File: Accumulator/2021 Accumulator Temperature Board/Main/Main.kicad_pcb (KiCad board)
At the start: 2 copper layers, 63.4 x 45.4 mm, 51 parts, among them J1 Conn_02x06_Odd_Even, J1001 Conn_01x06, J1002 M3, J1003 Conn_01x04, J1004 Conn_01x04, J1005 M3, J1006 M3, J2 Conn_02x06_Odd_Even, J3 M3, U20002 ISO1050, U20003 RFM-0505S, U2001 STM32F072R8Tx, U3001 LP2985-3.3

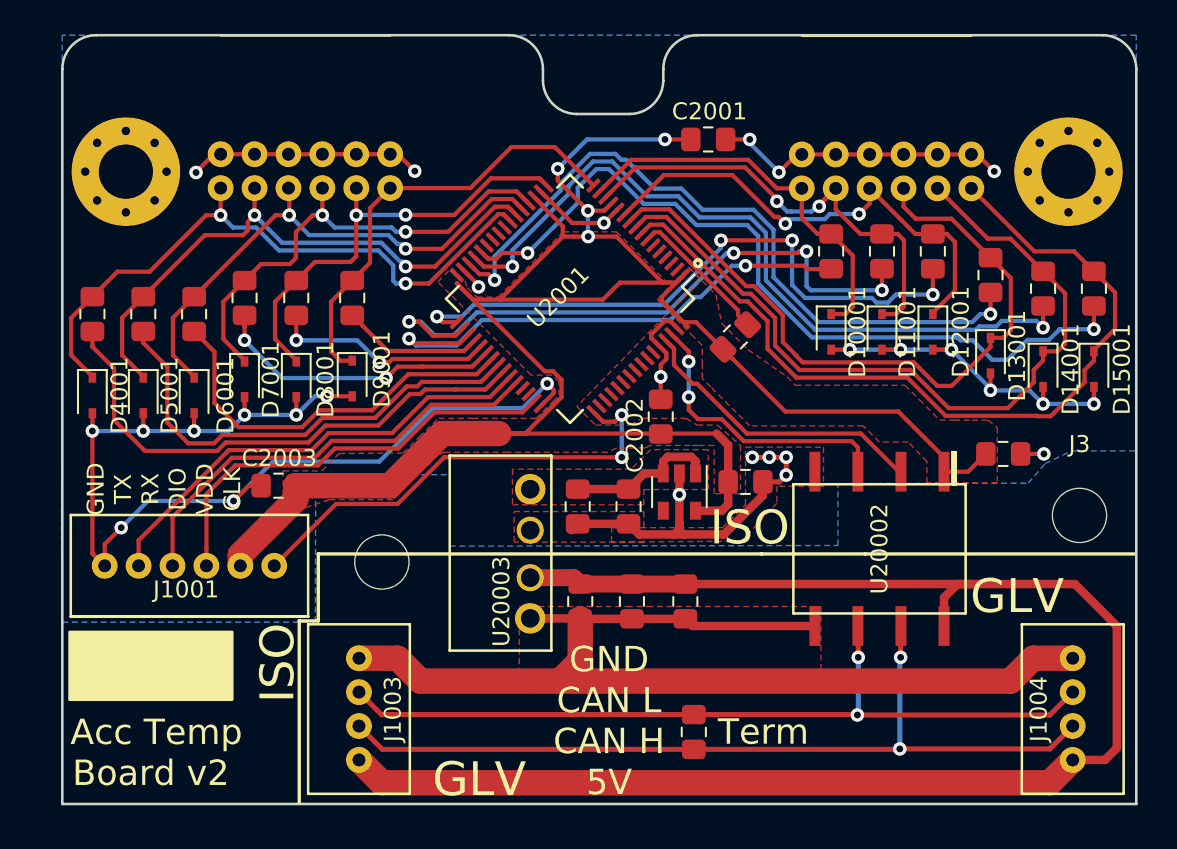
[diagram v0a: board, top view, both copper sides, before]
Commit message: Changes to Thermoboard
Disconnected mounting holes from GND, changed Zener package to hand-soldering.
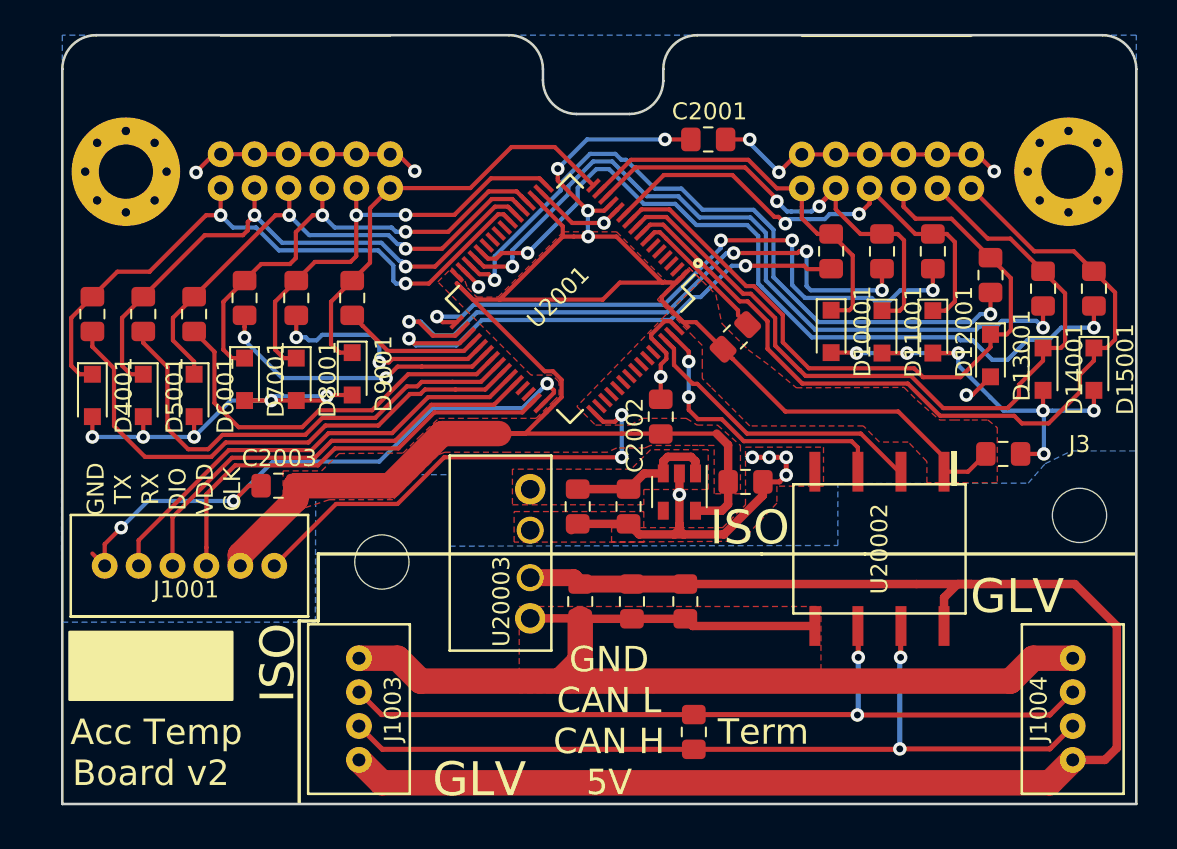
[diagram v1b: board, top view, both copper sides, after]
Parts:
- removed G***: LOGO, KiCAD Graphics:KiCAD_Duck_Graphic_v3
- removed G***: LOGO, KiCAD Graphics:UOWM_LOGO_v1
- D10001, D11001, D12001, D13001, D14001, D15001, D4001, D5001, D6001, D7001, D8001, D9001: footprint Diode_SMD:D_SOD-323 -> Diode_SMD:D_SOD-323_HandSoldering
- moved D9001 0.27 mm to (12.8, -38.1)
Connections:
- J1002 pad 1: GND -> Net-(J1002-Pad1)
- J1006 pad 1: GND -> Net-(J1006-Pad1)
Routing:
- net GND: track 155.7 -> 157.0 mm, vias 29 -> 28
- net /MUX Interface/ADC_11: track 49.9 -> 50.9 mm
- net /MUX Interface/PU_3: track 18.0 -> 17.1 mm
- net /MUX Interface/PU_4: track 13.3 -> 14.1 mm
- net /MUX Interface/ADC_5: track 27.1 -> 26.5 mm

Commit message: Changes to Thermoboard Mounting
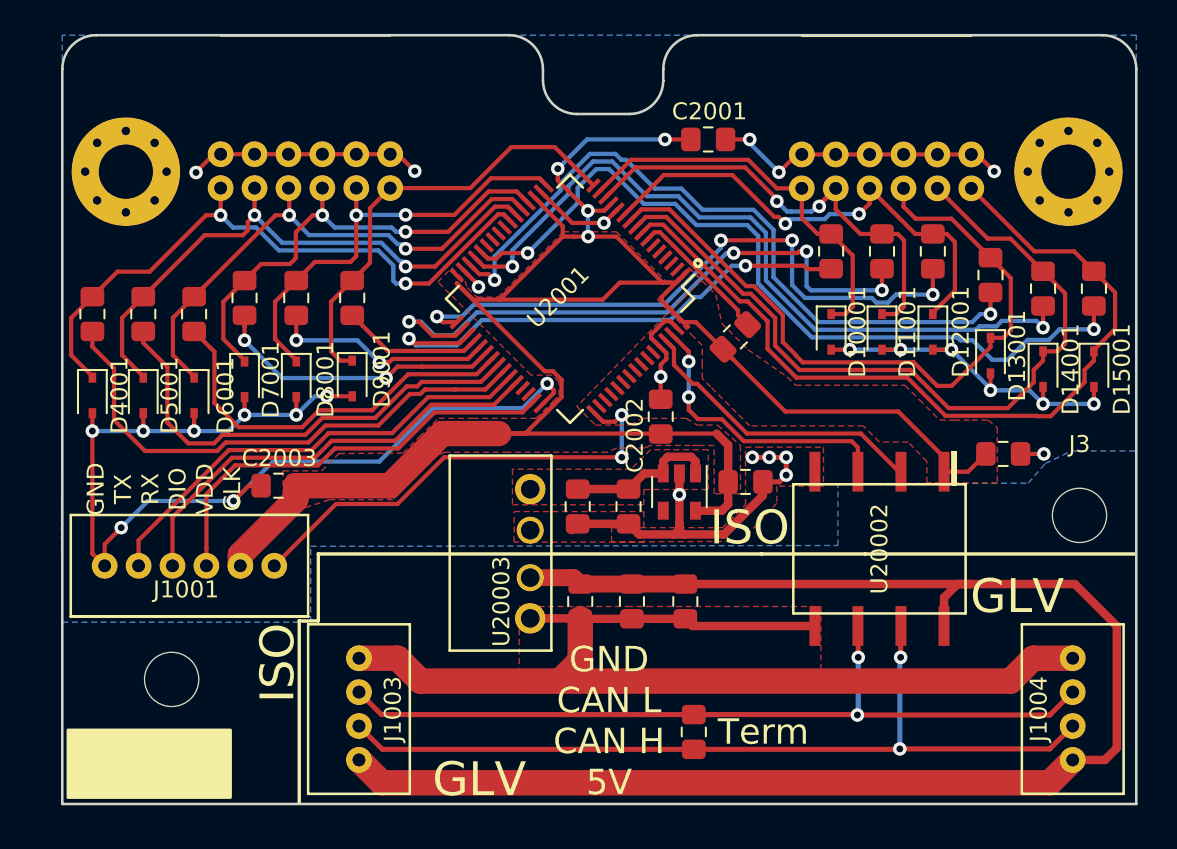
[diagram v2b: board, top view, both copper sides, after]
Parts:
- added G***: LOGO, KiCAD Graphics:UOWM_LOGO_v1, B.Cu at (38.9, -25.3)
- added G***: LOGO, KiCAD Graphics:KiCAD_Duck_Graphic_v3, B.Cu at (-1.98, -14.8)
- D10001, D11001, D12001, D13001, D14001, D15001, D4001, D5001, D6001, D7001, D8001, D9001: footprint Diode_SMD:D_SOD-323_HandSoldering -> Diode_SMD:D_SOD-323
- moved J1005 14.2 mm to (2.10, -20.1)
- moved D9001 0.27 mm to (12.8, -37.9)
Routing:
- net GND: track 157.0 -> 155.7 mm, vias 28 -> 29
- net /MUX Interface/ADC_11: track 50.9 -> 49.9 mm
- net /MUX Interface/PU_3: track 17.1 -> 18.0 mm
- net /MUX Interface/PU_4: track 14.1 -> 13.3 mm
- net /MUX Interface/ADC_5: track 26.5 -> 27.1 mm
